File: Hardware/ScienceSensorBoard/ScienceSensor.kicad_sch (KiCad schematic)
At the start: 94 parts, among them J1 Conn_02x03_Counter_Clockwise, J2 RJ45_LED_Shielded, Q1 SI4156DY, Q10 BSS138, Q11 SI4156DY, Q2 SI4156DY, Q3 SI4156DY, Q4 BSS138, Q5 BSS138, Q6 BSS138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

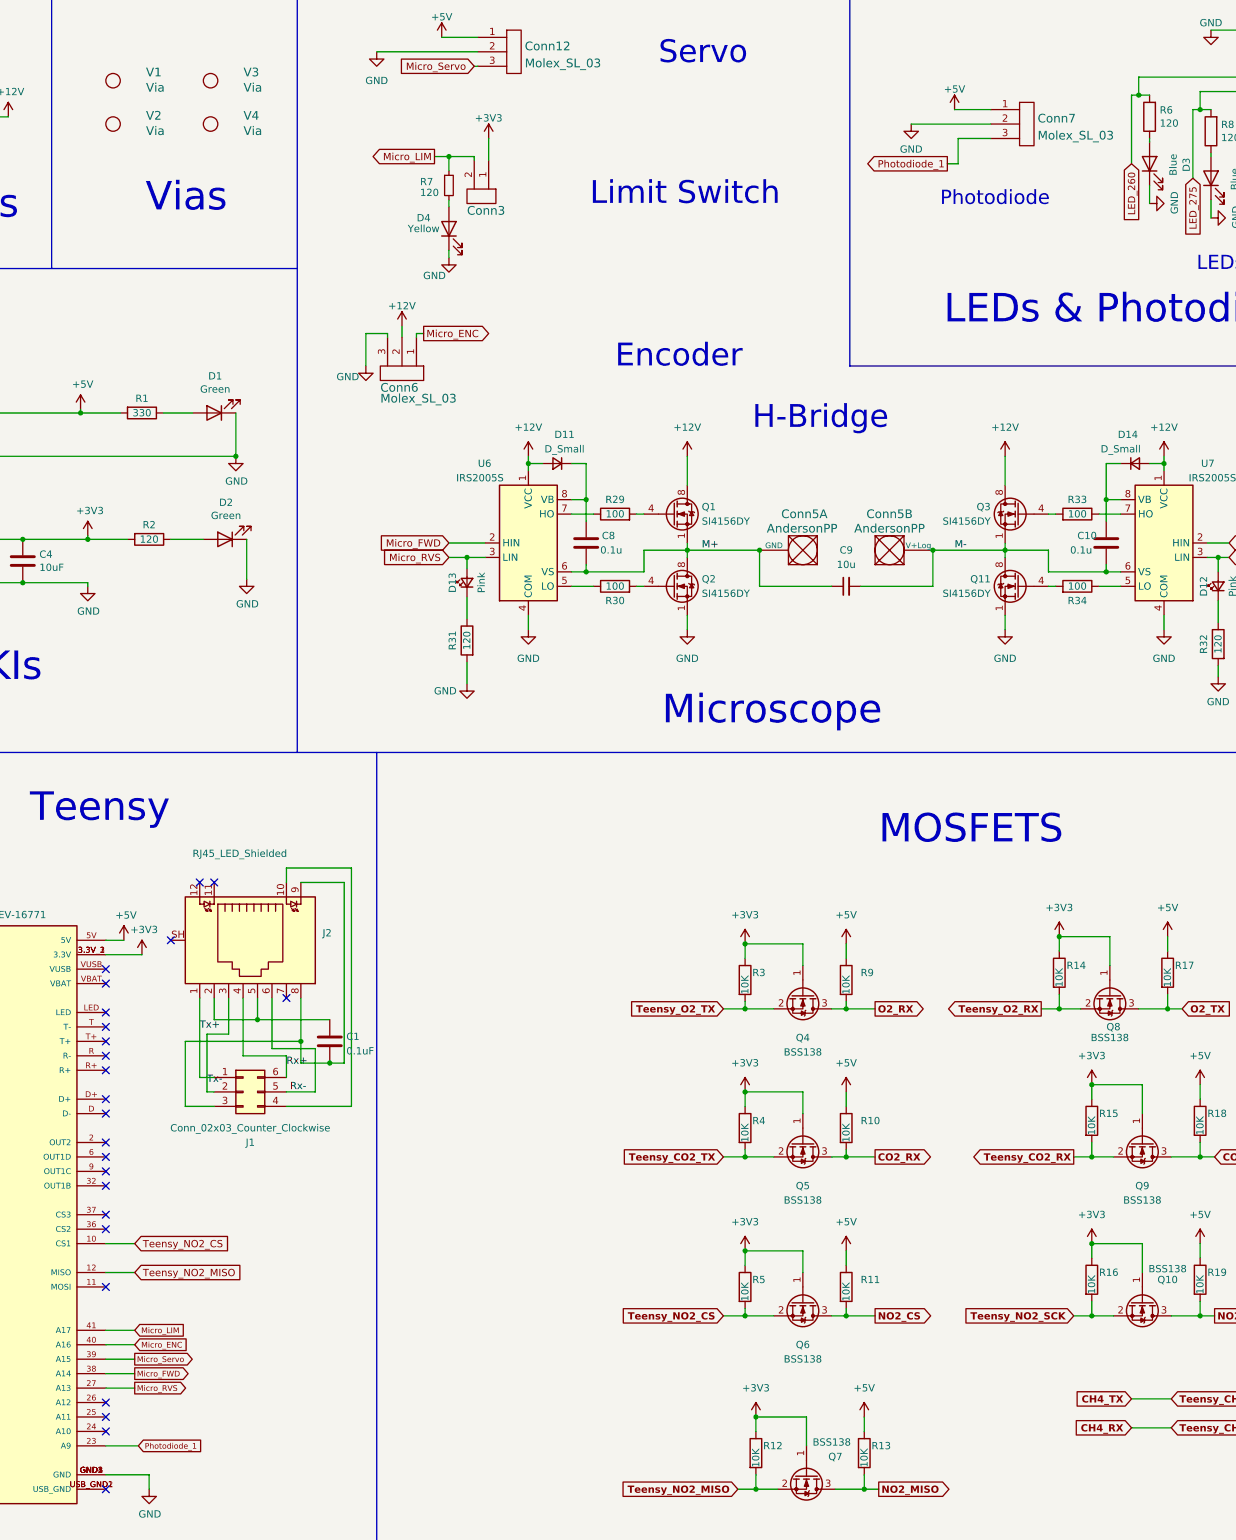
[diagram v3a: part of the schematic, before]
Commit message: Added 2nd Photodiode, Fixed OpAmp
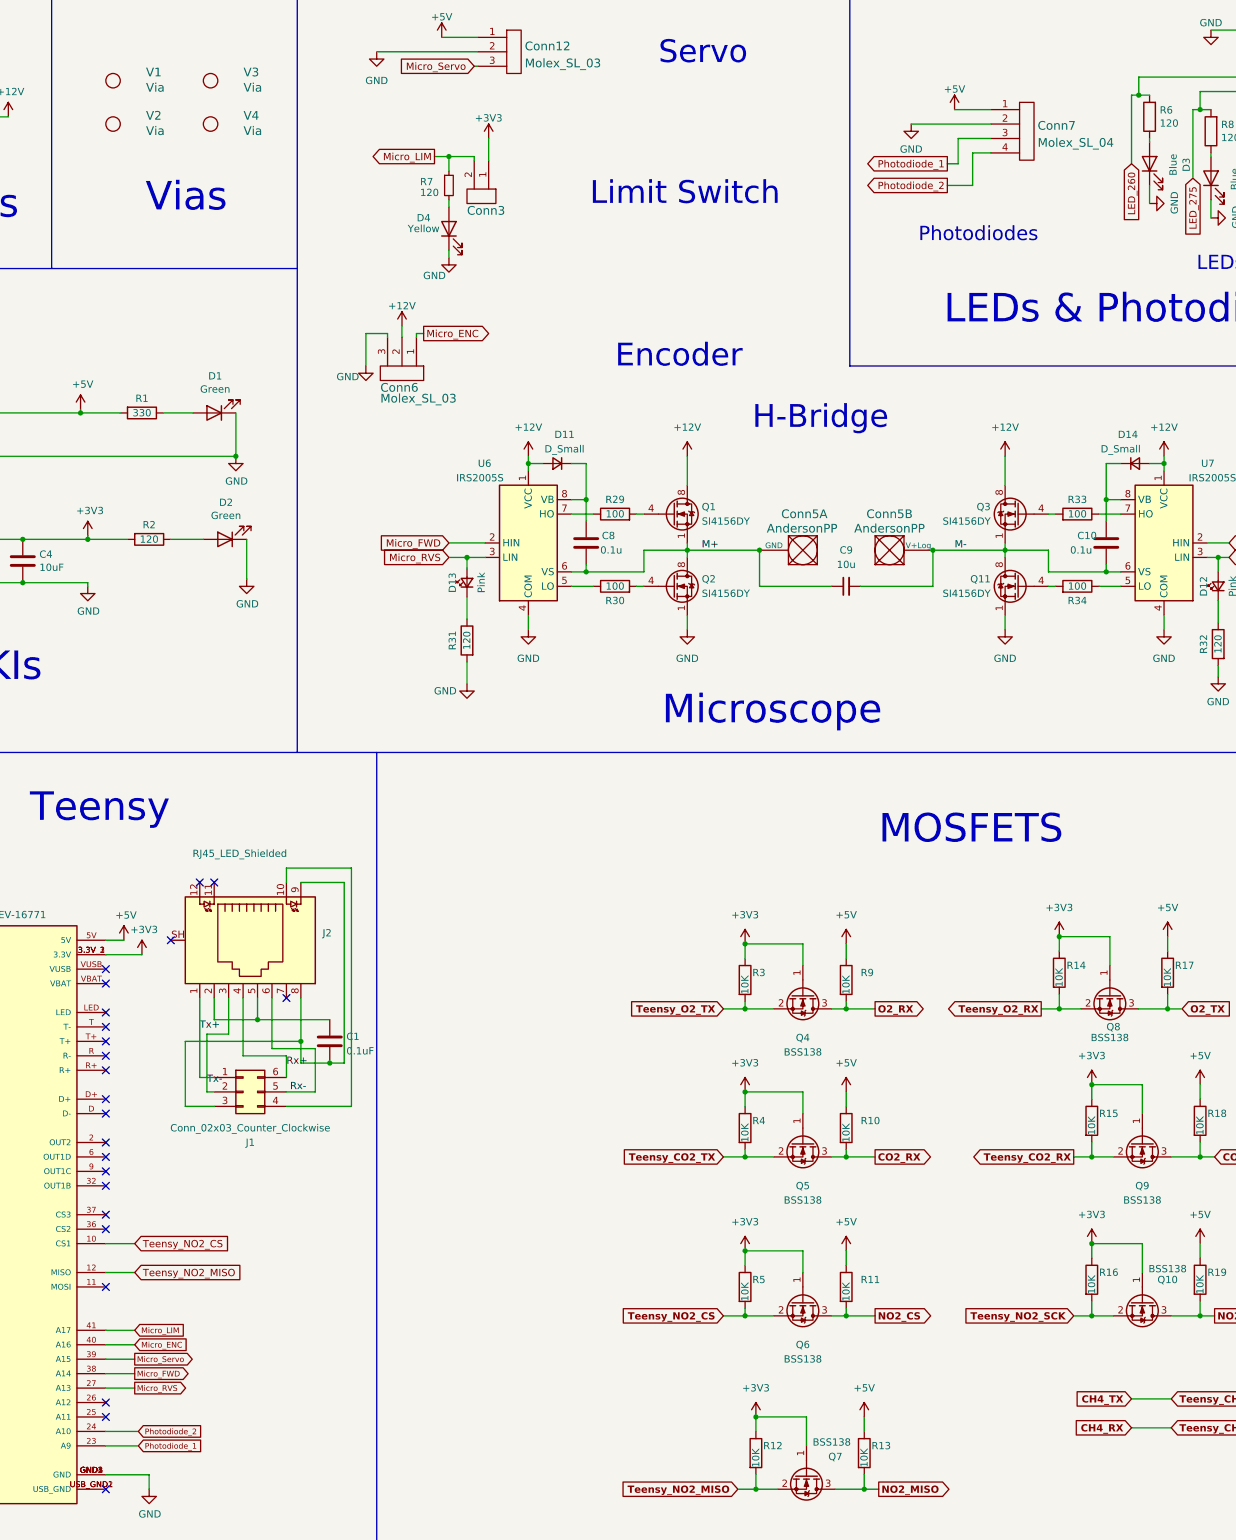
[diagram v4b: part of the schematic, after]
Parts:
- removed Conn7: Molex_SL_03, MRDT_Connectors:MOLEX_SL_03_Vertical, symbol MRDT_Connectors:Molex_SL_03
- added Conn7: Molex_SL_04, MRDT_Connectors:MOLEX_SL_04_Vertical, symbol MRDT_Connectors:Molex_SL_04
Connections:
- net +5V: now also Conn7.1
- net GND: now also Conn7.2
- net Photodiode_1: now also Conn7.3
- net Photodiode_2: now reaches U3.24 (A10)
- net Photodiode_2: now also Conn7.4
- no-connect marks 40 -> 39
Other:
- note added: "Photodiodes"
- note removed: "Photodiode"
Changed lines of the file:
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@@
   (no_connect (at 78.105 260.35))
   (no_connect (at 78.105 262.89))
-  (no_connect (at 78.105 265.43))
   (no_connect (at 94.615 168.91))
   (no_connect (at 97.155 168.91))
@@
     (stroke (width 0) (type default) (color 0 0 0 0))
   )
-  (wire (pts (xy 264.16 121.92) (xy 264.16 124.46))
-    (stroke (width 0) (type default) (color 0 0 0 0))
-  )
   (wire (pts (xy 369.57 38.735) (xy 369.57 36.83))
     (stroke (width 0) (type default) (color 0 0 0 0))
@@
     (stroke (width 0) (type default) (color 0 0 0 0))
   )
+  (wire (pts (xy 83.82 265.43) (xy 78.105 265.43))
+    (stroke (width 0) (type default) (color 0 0 0 0))
+  )
   (wire (pts (xy 227.965 38.1) (xy 227.965 42.545))
     (stroke (width 0) (type default) (color 0 0 0 0))
@@
     (stroke (width 0) (type default) (color 0 0 0 0))
   )
+  (wire (pts (xy 230.505 46.355) (xy 230.505 40.64))
+    (stroke (width 0) (type default) (color 0 0 0 0))
+  )
   (wire (pts (xy 95.885 205.74) (xy 95.885 195.58))
     (stroke (width 0) (type default) (color 0 0 0 0))
@@
     (stroke (width 0) (type default) (color 0 0 0 0))
   )
+  (wire (pts (xy 230.505 40.64) (xy 233.68 40.64))
+    (stroke (width 0) (type default) (color 0 0 0 0))
+  )
   (wire (pts (xy 109.855 199.39) (xy 102.235 199.39))
     (stroke (width 0) (type default) (color 0 0 0 0))
@@
     (stroke (width 0) (type default) (color 0 0 0 0))
   )
+  (wire (pts (xy 264.16 121.92) (xy 264.16 124.46))
+    (stroke (width 0) (type default) (color 0 0 0 0))
+  )
   (wire (pts (xy 360.68 76.835) (xy 361.95 76.835))
     (stroke (width 0) (type default) (color 0 0 0 0))
@@
     (stroke (width 0) (type default) (color 0 0 0 0))
   )
+  (wire (pts (xy 226.06 46.355) (xy 230.505 46.355))
+    (stroke (width 0) (type default) (color 0 0 0 0))
+  )
   (wire (pts (xy 109.855 205.74) (xy 114.935 205.74))
     (stroke (width 0) (type default) (color 0 0 0 0))
@@
     (effects (font (size 5 5)) (justify left bottom))
   )
-  (text "Photodiode" (at 224.79 50.165 0)
+  (text "Photodiodes" (at 220.98 56.515 0)
     (effects (font (size 2.5 2.5)) (justify left bottom))
   )
@@
     )
   )
+  (global_label "Photodiode_2" (shape input) (at 83.82 265.43 0) (fields_autoplaced)
+    (effects (font (size 0.9906 0.9906)) (justify left))
+    (property "Intersheet References" "${INTERSHEET_REFS}" (id 0) (at 95.5859 265.3681 0)
+      (effects (font (size 0.9906 0.9906)) (justify left) hide)
+    )
+  )
   (global_label "Micro_RVS" (shape input) (at 275.59 109.22 0) (fields_autoplaced)
     (effects (font (size 1.27 1.27)) (justify left))
@@
     )
   )
+  (global_label "Photodiode_2" (shape output) (at 226.06 46.355 180) (fields_autoplaced)
+    (effects (font (size 1.27 1.27)) (justify right))
+    (property "Intersheet References" "${INTERSHEET_REFS}" (id 0) (at 210.9753 46.2756 0)
+      (effects (font (size 1.27 1.27)) (justify right) hide)
+    )
+  )
   (global_label "LED_315" (shape output) (at 31.115 255.27 180) (fields_autoplaced)
     (effects (font (size 0.9906 0.9906)) (justify right))
@@
     (pin "2")
   )
-  (symbol (lib_id "MRDT_Connectors:Molex_SL_03") (at 238.76 39.37 0) (unit 1)
-    (in_bom yes) (on_board yes) (fields_autoplaced)
-    (property "Reference" "Conn7" (id 0) (at 241.935 34.5838 0)
-      (effects (font (size 1.524 1.524)) (justify left))
-    )
-    (property "Value" "Molex_SL_03" (id 1) (at 241.935 37.5772 0)
-      (effects (font (size 1.524 1.524)) (justify left))
-    )
-    (property "Footprint" "MRDT_Connectors:MOLEX_SL_03_Vertical" (id 2) (at 238.76 39.37 0)
-      (effects (font (size 1.524 1.524)) hide)
-    )
-    (property "Datasheet" "" (id 3) (at 238.76 39.37 0)
-      (effects (font (size 1.524 1.524)) hide)
-    )
-    (pin "1")
-    (pin "2")
-    (pin "3")
-  )
   (symbol (lib_id "power:+3V3") (at 192.405 262.89 0) (unit 1)
     (in_bom yes) (on_board yes) (fields_autoplaced)
@@
     (pin "2")
   )
+  (symbol (lib_id "MRDT_Connectors:Molex_SL_04") (at 238.76 41.91 0) (unit 1)
+    (in_bom yes) (on_board yes) (fields_autoplaced)
+    (property "Reference" "Conn7" (id 0) (at 241.935 35.8538 0)
+      (effects (font (size 1.524 1.524)) (justify left))
+    )
+    (property "Value" "Molex_SL_04" (id 1) (at 241.935 38.8472 0)
+      (effects (font (size 1.524 1.524)) (justify left))
+    )
+    (property "Footprint" "MRDT_Connectors:MOLEX_SL_04_Vertical" (id 2) (at 238.76 41.91 0)
+      (effects (font (size 1.524 1.524)) hide)
+    )
+    (property "Datasheet" "" (id 3) (at 238.76 41.91 0)
+      (effects (font (size 1.524 1.524)) hide)
+    )
+    (pin "1")
+    (pin "2")
+    (pin "3")
+    (pin "4")
+  )
   (symbol (lib_id "power:GND") (at 85.725 275.59 0) (unit 1)
     (in_bom yes) (on_board yes)
@@
       (reference "Conn6") (unit 1) (value "Molex_SL_03") (footprint "MRDT_Connectors:MOLEX_SL_03_Vertical")
     )
-    (path "/0801cfcf-c1b0-4c18-945f-084fcc49db23"
-      (reference "Conn7") (unit 1) (value "Molex_SL_03") (footprint "MRDT_Connectors:MOLEX_SL_03_Vertical")
+    (path "/17bdc4af-b7fd-461e-b9eb-6fab69389ac2"
+      (reference "Conn7") (unit 1) (value "Molex_SL_04") (footprint "MRDT_Connectors:MOLEX_SL_04_Vertical")
     )
     (path "/6a2e2e5d-609f-433a-995e-8e1ddb8bf56f"

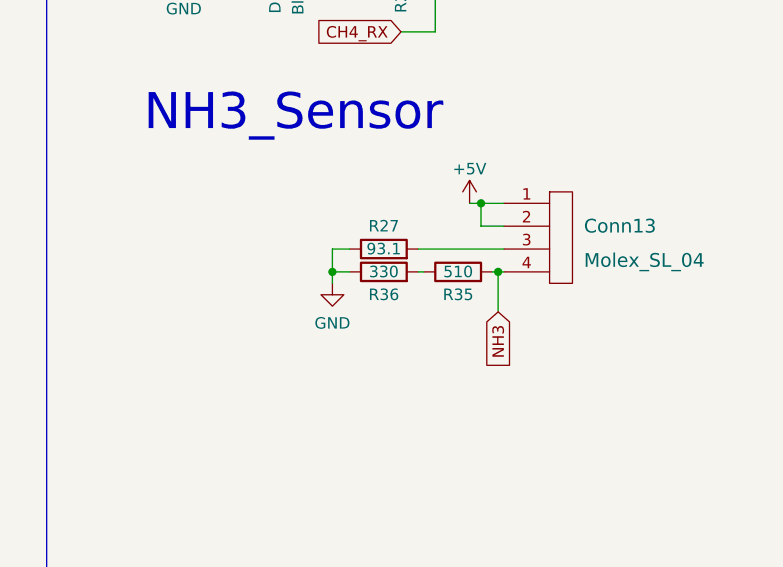
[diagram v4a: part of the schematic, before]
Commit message: Changed Measurement Resistance for NH3 sensor
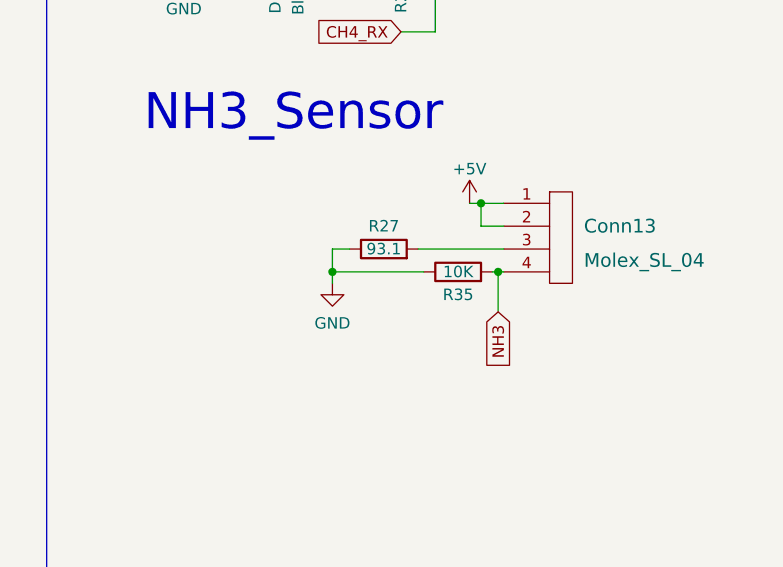
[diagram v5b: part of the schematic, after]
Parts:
- removed R36: 330, Resistor_SMD:R_0603_1608Metric_Pad0.98x0.95mm_HandSolder, symbol Device:R
- R35: value 510 -> 10K
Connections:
- net GND: now also R35.1
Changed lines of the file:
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@@
     (stroke (width 0) (type default) (color 0 0 0 0))
   )
-  (wire (pts (xy 348.615 184.15) (xy 350.52 184.15))
-    (stroke (width 0) (type default) (color 0 0 0 0))
-  )
   (wire (pts (xy 192.405 275.59) (xy 196.215 275.59))
     (stroke (width 0) (type default) (color 0 0 0 0))
@@
     (stroke (width 0) (type default) (color 0 0 0 0))
   )
-  (wire (pts (xy 358.14 184.15) (xy 358.775 184.15))
+  (wire (pts (xy 348.615 184.15) (xy 358.775 184.15))
     (stroke (width 0) (type default) (color 0 0 0 0))
   )
@@
     (in_bom yes) (on_board yes)
     (property "Reference" "R35" (id 0) (at 362.585 186.69 90))
-    (property "Value" "510" (id 1) (at 362.585 184.15 90))
+    (property "Value" "10K" (id 1) (at 362.585 184.15 90))
     (property "Footprint" "Resistor_SMD:R_0603_1608Metric_Pad0.98x0.95mm_HandSolder" (id 2) (at 362.585 185.928 90)
       (effects (font (size 1.27 1.27)) hide)
@@
     (pin "1")
   )
-  (symbol (lib_id "Device:R") (at 354.33 184.15 90) (unit 1)
-    (in_bom yes) (on_board yes)
-    (property "Reference" "R36" (id 0) (at 354.33 186.69 90))
-    (property "Value" "330" (id 1) (at 354.33 184.15 90))
-    (property "Footprint" "Resistor_SMD:R_0603_1608Metric_Pad0.98x0.95mm_HandSolder" (id 2) (at 354.33 185.928 90)
-      (effects (font (size 1.27 1.27)) hide)
-    )
-    (property "Datasheet" "~" (id 3) (at 354.33 184.15 0)
-      (effects (font (size 1.27 1.27)) hide)
-    )
-    (pin "1")
-    (pin "2")
-  )
   (symbol (lib_id "Transistor_FET:FDS2734") (at 177.8 104.14 0) (unit 1)
     (in_bom yes) (on_board yes)
@@
     )
     (path "/225ce1a4-00d7-45b6-bf5f-e3cf4f34a1ad"
-      (reference "R35") (unit 1) (value "510") (footprint "Resistor_SMD:R_0603_1608Metric_Pad0.98x0.95mm_HandSolder")
-    )
-    (path "/3d394b4d-5c79-4696-914b-1adabca0d60d"
-      (reference "R36") (unit 1) (value "330") (footprint "Resistor_SMD:R_0603_1608Metric_Pad0.98x0.95mm_HandSolder")
+      (reference "R35") (unit 1) (value "10K") (footprint "Resistor_SMD:R_0603_1608Metric_Pad0.98x0.95mm_HandSolder")
     )
     (path "/c5bc5e0f-59b7-45b6-b17c-1888cdf8bc2c"
